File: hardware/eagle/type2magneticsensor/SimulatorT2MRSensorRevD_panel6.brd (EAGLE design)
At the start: 99.1 x 96.5 mm, 61 parts

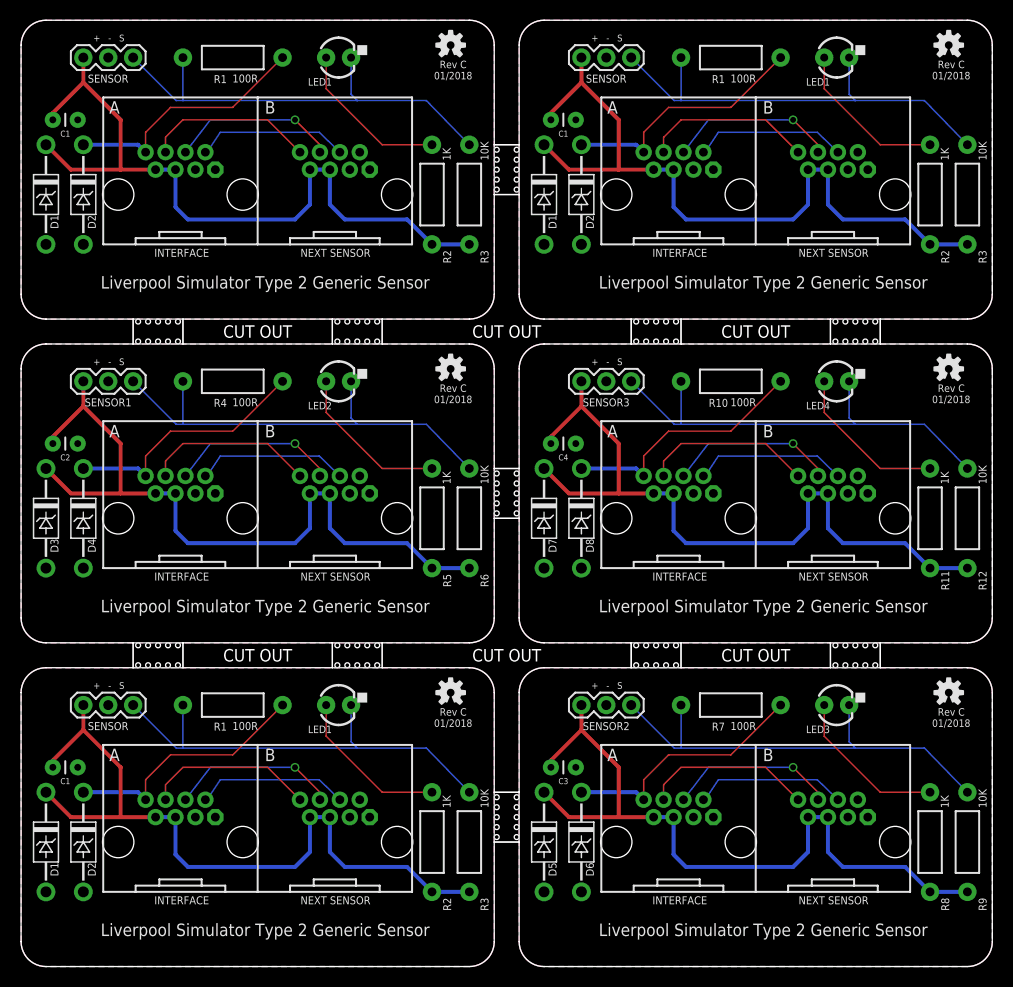
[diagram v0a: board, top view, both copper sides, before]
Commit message: Board Housekeeping
URL on silkscreens, caution messages, tidy up naming conventions.
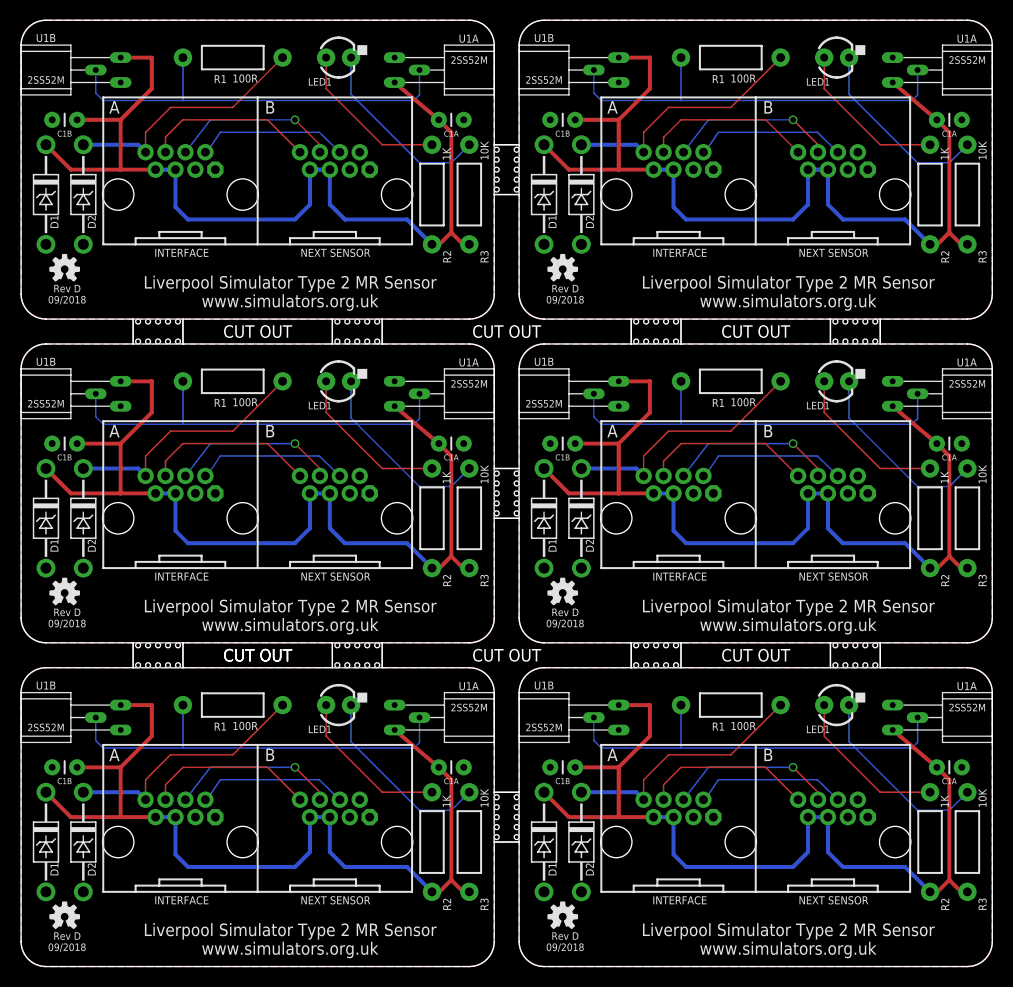
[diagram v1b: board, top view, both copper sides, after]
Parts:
- removed C1, C1_1, C1_2, C2, C3, C4: 100nF, SparkFun-Passives:CAP-PTH-SMALL
- removed D3, D4: SA5.0A, AIC_Custom:DO41_TVS_UNI
- removed JP2: RJ45-RJHSE-5080-023HOLE, AIC_Custom:RJ45-RJHSE-5080-02-3HOLE
- removed LED2: Blue, SparkFun-LED:LED3MM
- removed LOGO2, LOGO3, LOGO4: OSHW-LOGOS, SparkFun-Aesthetics:OSHW-LOGO-S
- removed R4: 100R, SparkFun-Passives:AXIAL-0.4
- removed R5: 1K, SparkFun-Passives:AXIAL-0.4
- removed R6: 10K, SparkFun-Passives:AXIAL-0.4
- removed SENSOR, SENSOR1, SENSOR2, SENSOR3, SENSOR_1, SENSOR_2: (no value), SparkFun-Connectors:1X03
- added C1A, C1A_1, C1A_2, C1A_3, C1A_4, C1A_5, C1B, C1B_1, C1B_2, C1B_3, C1B_4, C1B_5: 100nF, SparkFun-Passives:CAP-PTH-SMALL
- added D1_5, D2_5: SA5.0A, AIC_Custom:DO41_TVS_UNI
- added E$12: (no value), AIC_Custom:OUTLINE_PANEL_6_5MM
- added E$2, E$3, E$4, E$5, E$6: (no value), AIC_Custom:WARNING_TRIANGLE_TPLACE
- added JP1_5: RJ45-RJHSE-5080-023HOLE, AIC_Custom:RJ45-RJHSE-5080-02-3HOLE
- added LED1_5: Blue, SparkFun-LED:LED3MM
- added LOGO1_3, LOGO1_4, LOGO1_5: OSHW-LOGOS, SparkFun-Aesthetics:OSHW-LOGO-S
- added R1_5: 100R, SparkFun-Passives:AXIAL-0.4
- added R2_5: 1K, SparkFun-Passives:AXIAL-0.4
- added R3_5: 10K, SparkFun-Passives:AXIAL-0.4
- added U1A, U1A_1, U1A_2, U1A_3, U1A_4, U1A_5, U1B, U1B_1, U1B_2, U1B_3, U1B_4, U1B_5: 2SS52MOFFSET, AIC_Custom:2SS52M_FLAT_OFFSET
- E$1: device AIC_Custom:OUTLINE_PANEL_6_5MM -> AIC_Custom:WARNING_TRIANGLE_TPLACE
- moved LOGO1_2 93.0 mm to (4.45, 71.1)
- moved LOGO1_1 68.4 mm to (4.45, 38.1)
- moved JP1_2 50.8 mm to (24.1, 78.7)
- moved D1_2 50.8 mm to (2.54, 78.7)
- moved LED1_2 50.8 mm to (32.4, 92.7)
- moved D2_2 50.8 mm to (6.35, 78.7)
- moved R1_2 50.8 mm to (21.6, 92.7)
- moved R2_2 50.8 mm to (41.9, 78.7)
- moved R3_2 50.8 mm to (45.7, 78.7)
- moved LOGO1 45.5 mm to (4.45, 5.08)
- moved E$1 38.3 mm to (38.1, 3.81), flipped to the bottom
- moved D1_1 33.0 mm to (2.54, 45.7)
- moved D2_1 33.0 mm to (6.35, 45.7)
- moved JP1_1 33.0 mm to (24.1, 45.7)
- moved LED1_1 33.0 mm to (32.4, 59.7)
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- renumbered D5 to D1_3, D6 to D2_3, D7 to D1_4, D8 to D2_4, JP3 to JP1_3, JP4 to JP1_4, LED3 to LED1_3, LED4 to LED1_4, R10 to R1_4, R11 to R2_4, R12 to R3_4, R7 to R1_3, R8 to R2_3, R9 to R3_3
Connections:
- net B10 renamed B24
- net B11 renamed B34
- net B12 renamed B44
- net B7 renamed B23
- net B8 renamed B33
- net B9 renamed B43
- removed net B1: JP2.A6, JP2.B8
- removed net B5: JP2.A4, JP2.B6
- removed net B6: JP2.A2, JP2.B4
- new net B25: JP1_5.A6, JP1_5.B8
- new net B35: JP1_5.A4, JP1_5.B6
- new net B45: JP1_5.A2, JP1_5.B4
- net !OUT!1: now also D2_1.CATHODE, JP1_1.A8, R1_1.P$1; no longer D4.CATHODE, JP2.A8, R4.P$1
- net !OUT!2: now also D2_2.CATHODE, JP1_2.A8, R1_2.P$1; no longer D2_3.CATHODE, JP1_3.A8, R1_3.P$1
- net !OUT!3: now also D2_3.CATHODE, JP1_3.A8, R1_3.P$1; no longer D2_4.CATHODE, JP1_4.A8, R1_4.P$1
- net !OUT!4: now also D2_4.CATHODE, JP1_4.A8, R1_4.P$1; no longer D2_1.CATHODE, JP1_1.A8, R1_1.P$1
- net !OUT!5: now also D2_5.CATHODE, JP1_5.A8, R1_5.P$1; no longer D2_2.CATHODE, JP1_2.A8, R1_2.P$1
- net GND: now also C1A.2, C1B.2, U1A.P$1, U1B.P$1; no longer C1.2, SENSOR.2
- net GND1: now also C1A_1.2, C1B_1.2, D1_1.ANODE, D2_1.ANODE, JP1_1.A1, JP1_1.A3, JP1_1.B1, JP1_1.B3, U1A_1.P$1, U1B_1.P$1; no longer C2.2, D3.ANODE, D4.ANODE, JP2.A1, JP2.A3, JP2.B1, JP2.B3, SENSOR1.2
- net GND2: now also C1A_2.2, C1B_2.2, D1_2.ANODE, D2_2.ANODE, JP1_2.A1, JP1_2.A3, JP1_2.B1, JP1_2.B3, U1A_2.P$1, U1B_2.P$1; no longer C3.2, D1_3.ANODE, D2_3.ANODE, JP1_3.A1, JP1_3.A3, JP1_3.B1, JP1_3.B3, SENSOR2.2
- net GND3: now also C1A_3.2, C1B_3.2, D1_3.ANODE, D2_3.ANODE, JP1_3.A1, JP1_3.A3, JP1_3.B1, JP1_3.B3, U1A_3.P$1, U1B_3.P$1; no longer C4.2, D1_4.ANODE, D2_4.ANODE, JP1_4.A1, JP1_4.A3, JP1_4.B1, JP1_4.B3, SENSOR3.2
- net GND4: now also C1A_4.2, C1B_4.2, D1_4.ANODE, D2_4.ANODE, JP1_4.A1, JP1_4.A3, JP1_4.B1, JP1_4.B3, U1A_4.P$1, U1B_4.P$1; no longer C1_1.2, D1_1.ANODE, D2_1.ANODE, JP1_1.A1, JP1_1.A3, JP1_1.B1, JP1_1.B3, SENSOR_1.2
- net GND5: now also C1A_5.2, C1B_5.2, D1_5.ANODE, D2_5.ANODE, JP1_5.A1, JP1_5.A3, JP1_5.B1, JP1_5.B3, U1A_5.P$1, U1B_5.P$1; no longer C1_2.2, D1_2.ANODE, D2_2.ANODE, JP1_2.A1, JP1_2.A3, JP1_2.B1, JP1_2.B3, SENSOR_2.2
- net LED1: now also LED1_1.A, R2_1.P$1; no longer LED2.A, R5.P$1
- net LED2: now also LED1_2.A, R2_2.P$1; no longer LED1_3.A, R2_3.P$1
- net LED3: now also LED1_3.A, R2_3.P$1; no longer LED1_4.A, R2_4.P$1
- net LED4: now also LED1_4.A, R2_4.P$1; no longer LED1_1.A, R2_1.P$1
- net LED5: now also LED1_5.A, R2_5.P$1; no longer LED1_2.A, R2_2.P$1
- net SIG: now also U1A.P$2, U1B.P$2; no longer SENSOR.3
- net SIG1: now also LED1_1.K, R1_1.P$2, R3_1.P$1, U1A_1.P$2, U1B_1.P$2; no longer LED2.K, R4.P$2, R6.P$1, SENSOR1.3
- net SIG2: now also LED1_2.K, R1_2.P$2, R3_2.P$1, U1A_2.P$2, U1B_2.P$2; no longer LED1_3.K, R1_3.P$2, R3_3.P$1, SENSOR2.3
- net SIG3: now also LED1_3.K, R1_3.P$2, R3_3.P$1, U1A_3.P$2, U1B_3.P$2; no longer LED1_4.K, R1_4.P$2, R3_4.P$1, SENSOR3.3
- net SIG4: now also LED1_4.K, R1_4.P$2, R3_4.P$1, U1A_4.P$2, U1B_4.P$2; no longer LED1_1.K, R1_1.P$2, R3_1.P$1, SENSOR_1.3
- net SIG5: now also LED1_5.K, R1_5.P$2, R3_5.P$1, U1A_5.P$2, U1B_5.P$2; no longer LED1_2.K, R1_2.P$2, R3_2.P$1, SENSOR_2.3
- net VCC: now also C1A.1, C1B.1, U1A.P$3, U1B.P$3; no longer C1.1, SENSOR.1
- net VCC1: now also C1A_1.1, C1B_1.1, D1_1.CATHODE, JP1_1.A5, JP1_1.A7, JP1_1.B5, JP1_1.B7, R2_1.P$2, R3_1.P$2, U1A_1.P$3, U1B_1.P$3; no longer C2.1, D3.CATHODE, JP2.A5, JP2.A7, JP2.B5, JP2.B7, R5.P$2, R6.P$2, SENSOR1.1
- net VCC2: now also C1A_2.1, C1B_2.1, D1_2.CATHODE, JP1_2.A5, JP1_2.A7, JP1_2.B5, JP1_2.B7, R2_2.P$2, R3_2.P$2, U1A_2.P$3, U1B_2.P$3; no longer C3.1, D1_3.CATHODE, JP1_3.A5, JP1_3.A7, JP1_3.B5, JP1_3.B7, R2_3.P$2, R3_3.P$2, SENSOR2.1
- net VCC3: now also C1A_3.1, C1B_3.1, D1_3.CATHODE, JP1_3.A5, JP1_3.A7, JP1_3.B5, JP1_3.B7, R2_3.P$2, R3_3.P$2, U1A_3.P$3, U1B_3.P$3; no longer C4.1, D1_4.CATHODE, JP1_4.A5, JP1_4.A7, JP1_4.B5, JP1_4.B7, R2_4.P$2, R3_4.P$2, SENSOR3.1
- net VCC4: now also C1A_4.1, C1B_4.1, D1_4.CATHODE, JP1_4.A5, JP1_4.A7, JP1_4.B5, JP1_4.B7, R2_4.P$2, R3_4.P$2, U1A_4.P$3, U1B_4.P$3; no longer C1_1.1, D1_1.CATHODE, JP1_1.A5, JP1_1.A7, JP1_1.B5, JP1_1.B7, R2_1.P$2, R3_1.P$2, SENSOR_1.1
- net VCC5: now also C1A_5.1, C1B_5.1, D1_5.CATHODE, JP1_5.A5, JP1_5.A7, JP1_5.B5, JP1_5.B7, R2_5.P$2, R3_5.P$2, U1A_5.P$3, U1B_5.P$3; no longer C1_2.1, D1_2.CATHODE, JP1_2.A5, JP1_2.A7, JP1_2.B5, JP1_2.B7, R2_2.P$2, R3_2.P$2, SENSOR_2.1
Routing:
- net VCC5: track 76.1 -> 97.3 mm
- net VCC4: track 76.1 -> 97.3 mm
- net VCC1: track 76.1 -> 97.3 mm
- net VCC: track 76.1 -> 97.3 mm
- net VCC3: track 76.1 -> 97.3 mm
- net VCC2: track 76.1 -> 97.3 mm
- net B1: track 17.3 -> 0.00 mm
- net B25: track 0.00 -> 17.3 mm
- net B5: track 17.2 -> 0.00 mm, vias 1 -> 0
- net B35: track 0.00 -> 17.2 mm, vias 0 -> 1
- net B6: track 15.6 -> 0.00 mm
- net B45: track 0.00 -> 15.6 mm
- net SIG3: track 47.0 -> 62.3 mm
- net SIG4: track 47.0 -> 62.3 mm
- net SIG1: track 47.0 -> 62.3 mm
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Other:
- board text added: "2SS52M Lead Forming Guide"
- board text added: "C1A"
- board text added: "C1B"
- board text added: "CUT OUT"
- board text added: "Connect this board to Liverpool Simulator Type 2 or compatible equipment ONLY. Refer to documentation for details."
- board text added: "Liverpool Simulator Type 2 MR Sensor www.simulators.org.uk"
- board text added: "Rev D 09/2018"
- board text added: "U1A"
- board text added: "U1B"
- board text removed: "+ - S"
- board text removed: "C1"
- board text removed: "Liverpool Simulator Type 2 Generic Sensor"
- board text removed: "Rev C 01/2018"
- board text removed: "SENSOR"
